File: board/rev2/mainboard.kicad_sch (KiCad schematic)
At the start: 0 parts

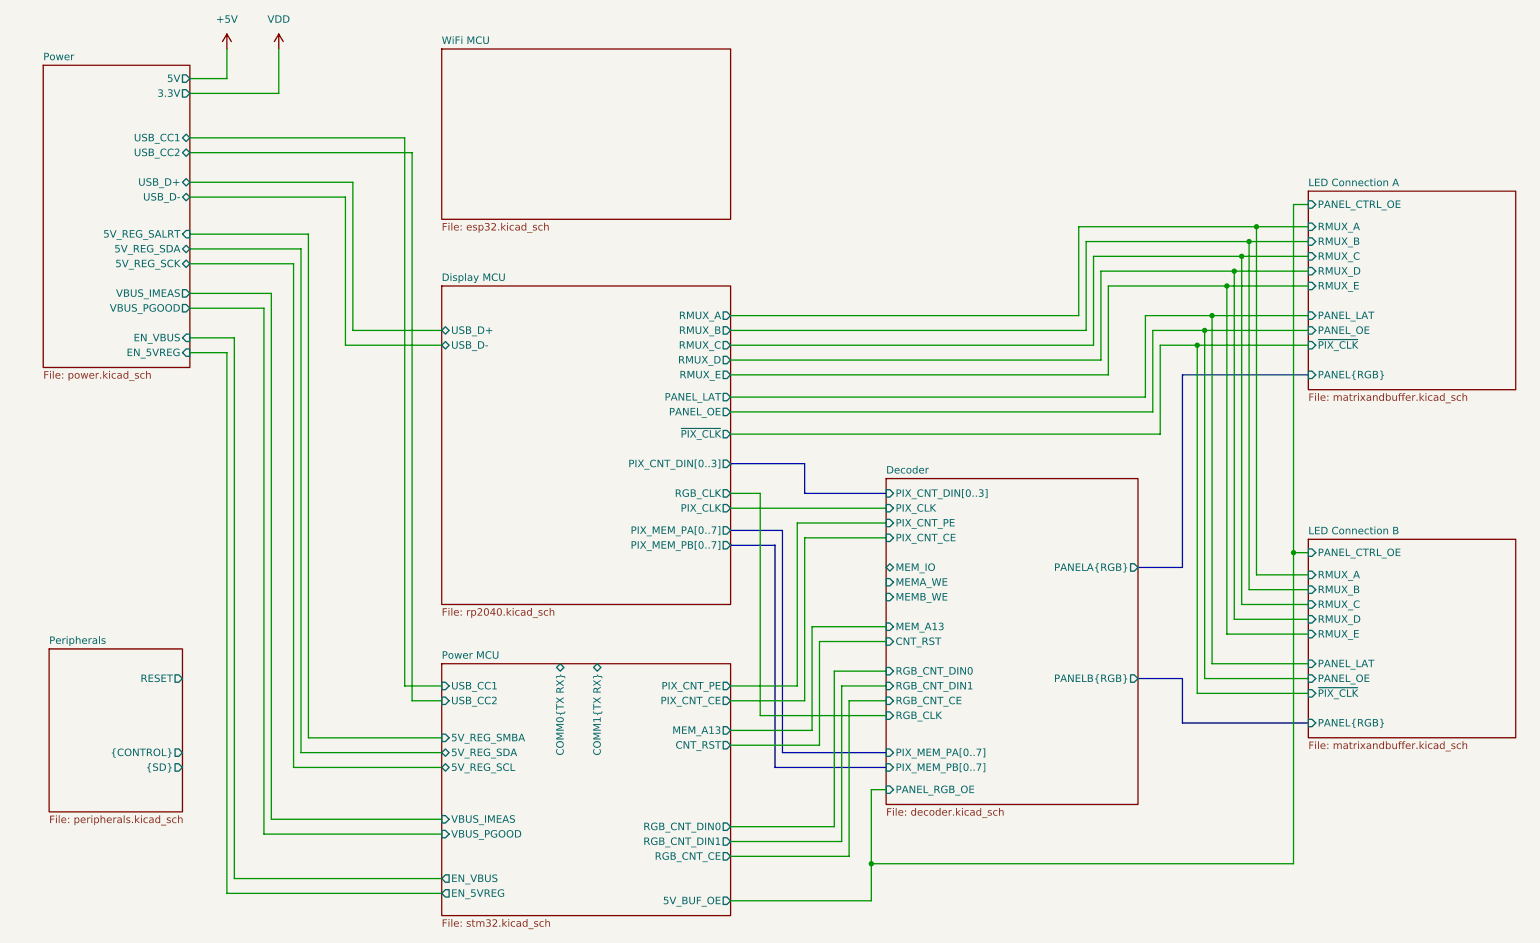
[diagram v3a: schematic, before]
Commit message: Board GPIO allocation
- and usbmux

still need to do termination on the big buses + a bunch of bypass caps
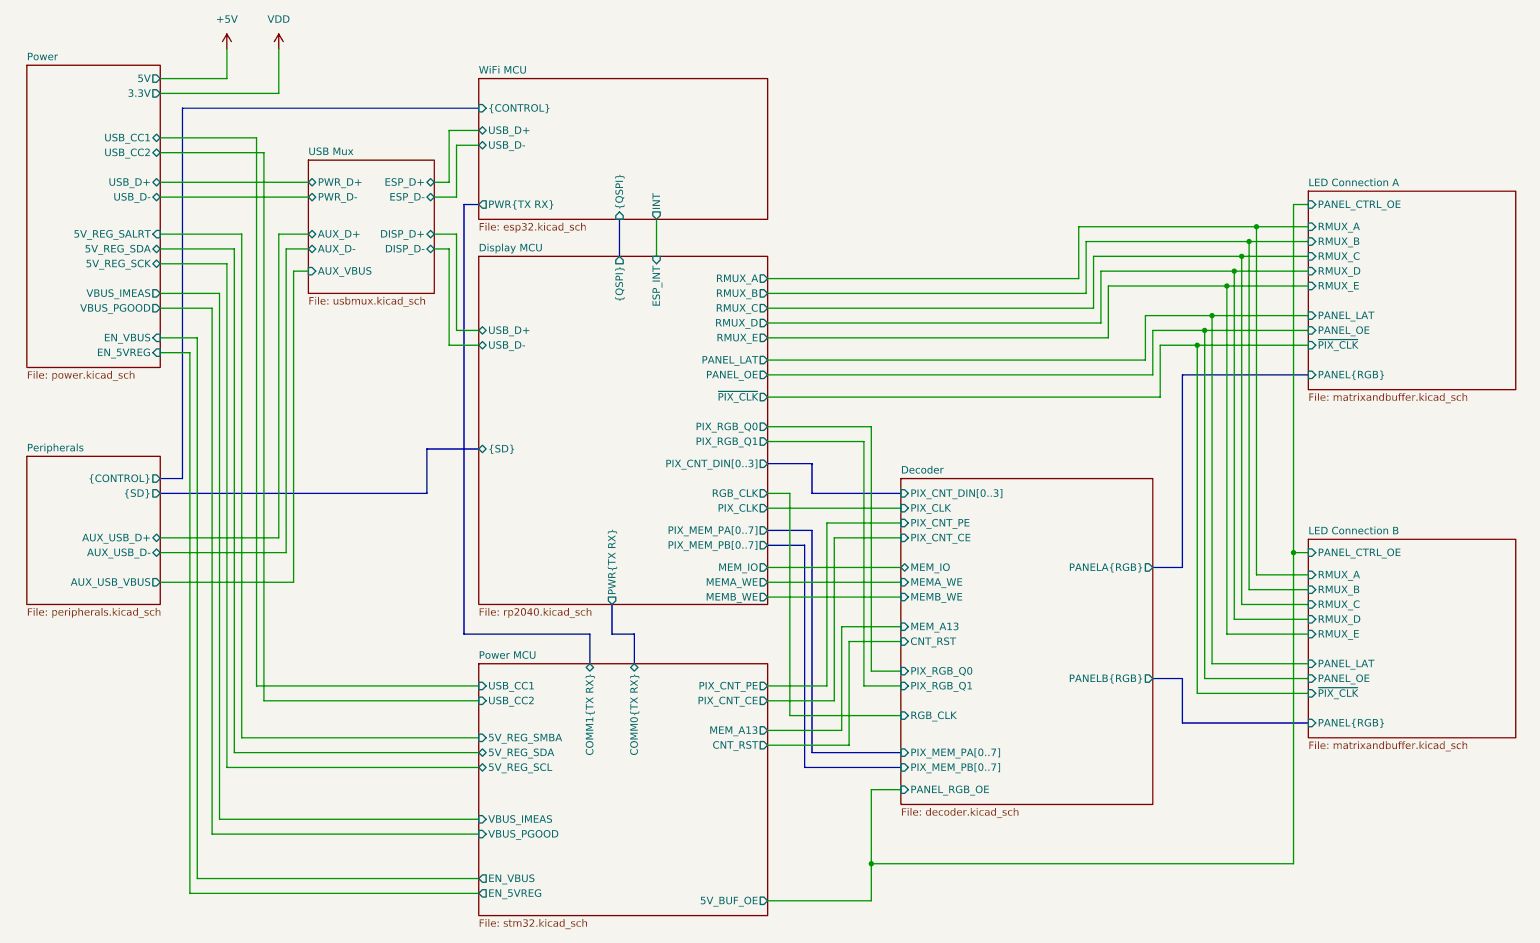
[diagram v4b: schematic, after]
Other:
- added sheet USB Mux (usbmux.kicad_sch)
- sheet Decoder ports: added PIX_RGB_Q0, PIX_RGB_Q1; removed RGB_CNT_CE, RGB_CNT_DIN0, RGB_CNT_DIN1
- sheet Display MCU ports: added ESP_INT, MEMA_WE, MEMB_WE, MEM_IO, PIX_RGB_Q0, PIX_RGB_Q1, PWR{TX RX}, {QSPI}, {SD}; removed none
- sheet Peripherals ports: added AUX_USB_D+, AUX_USB_D-, AUX_USB_VBUS; removed RESET
- sheet Power MCU ports: added none; removed RGB_CNT_CE, RGB_CNT_DIN0, RGB_CNT_DIN1
- sheet WiFi MCU ports: added INT, PWR{TX RX}, USB_D+, USB_D-, {CONTROL}, {QSPI}; removed none
- company: (none) -> MLABS
- title: (none) -> Root

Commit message: Continue board, assign caps/res, adjust for JLC availability
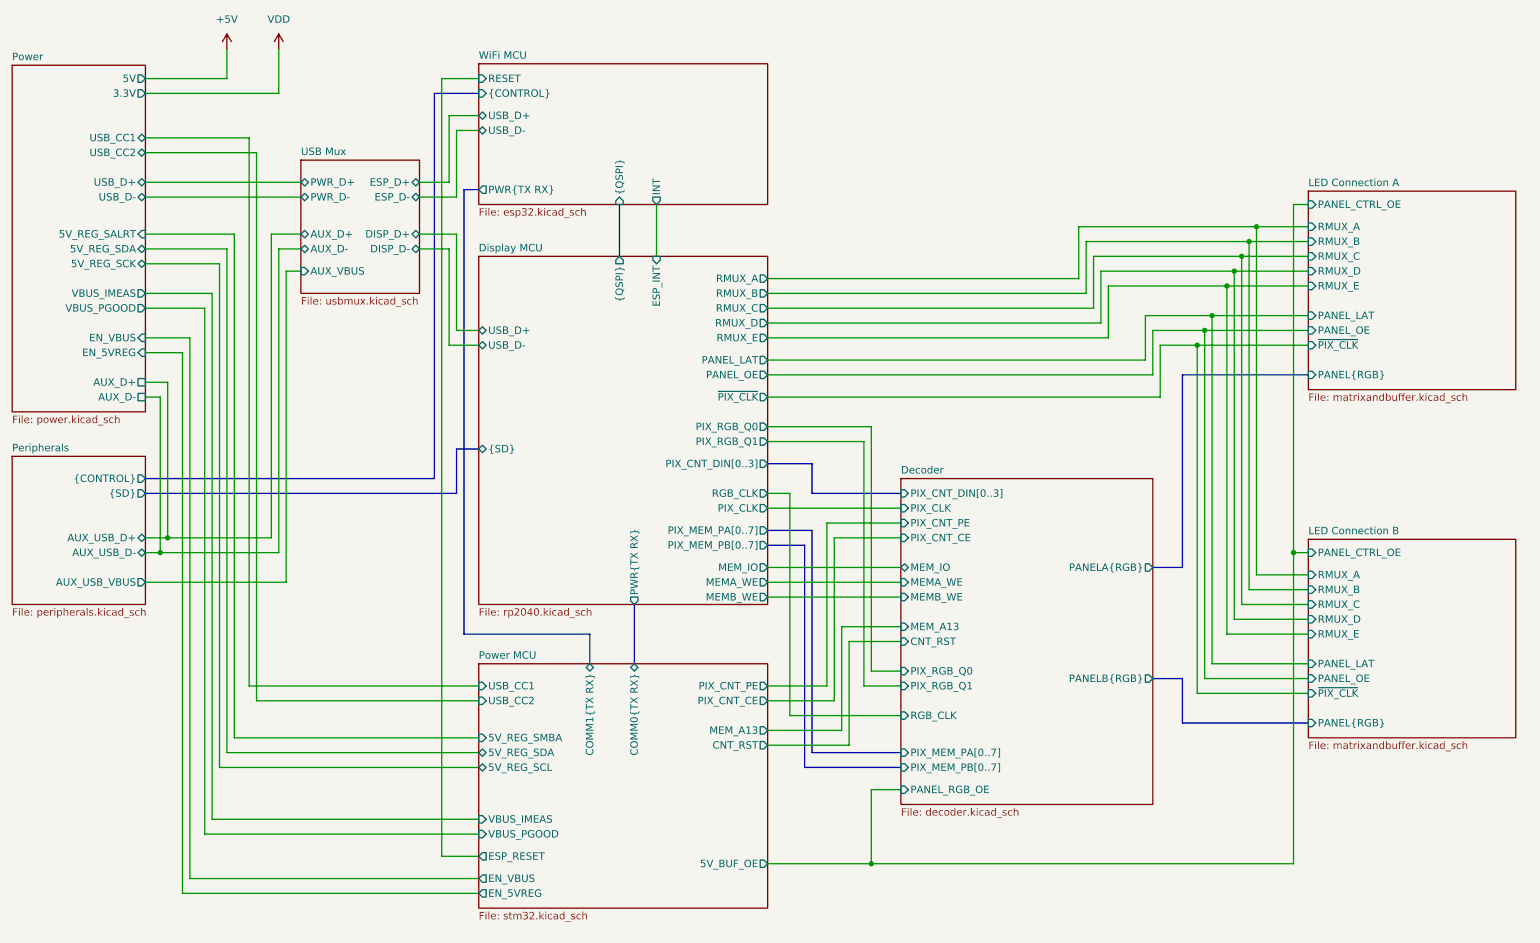
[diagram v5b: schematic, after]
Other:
- sheet Power ports: added AUX_D+, AUX_D-; removed none
- sheet Power MCU ports: added ESP_RESET; removed none
- sheet WiFi MCU ports: added RESET; removed none

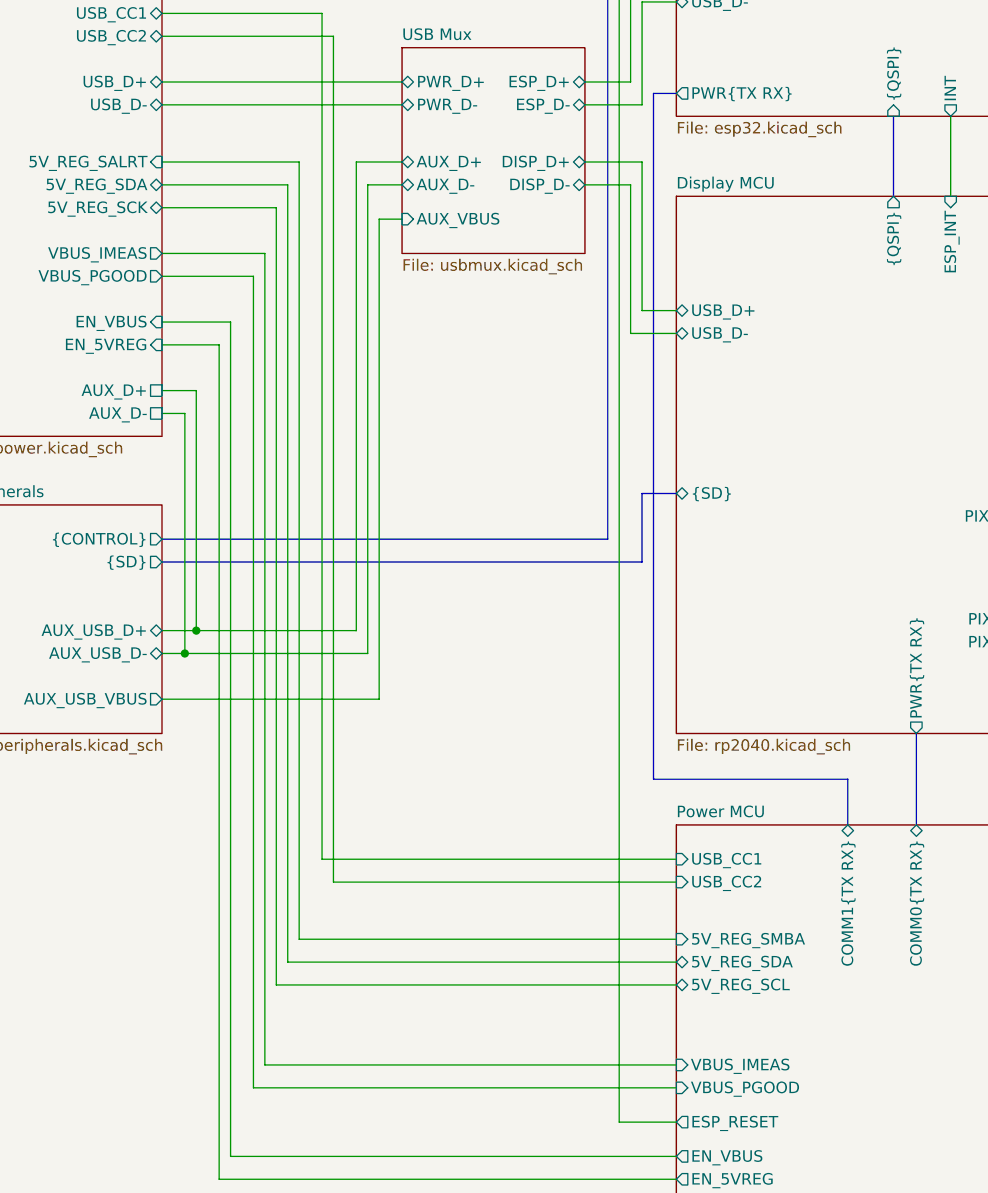
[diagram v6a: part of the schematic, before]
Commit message: Add netclasses, more footprints, fix ERC
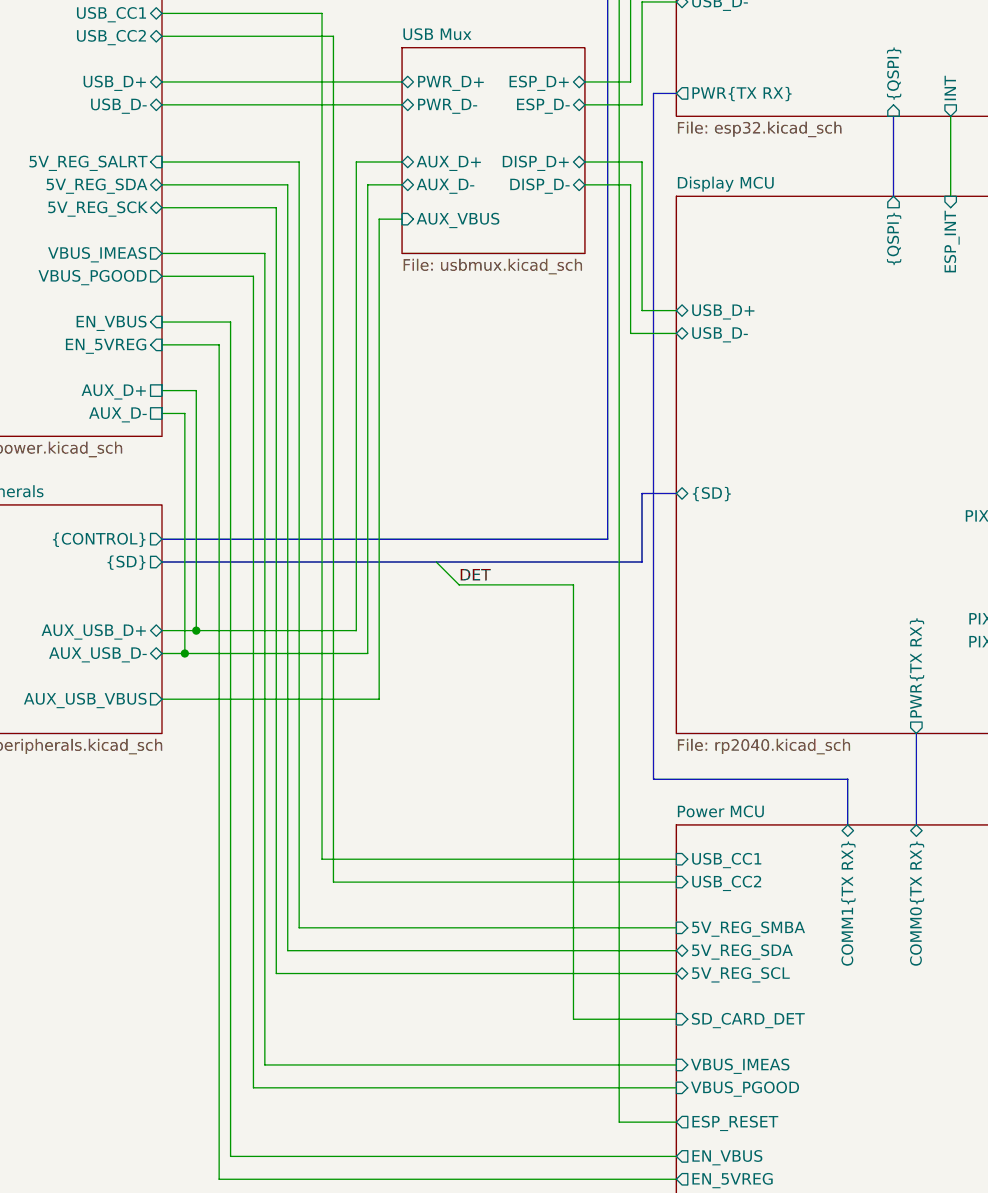
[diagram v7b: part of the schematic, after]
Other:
- sheet Power MCU ports: added SD_CARD_DET; removed none
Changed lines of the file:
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@@
 		(color 0 0 0 0)
 	)
+	(bus_entry
+		(at 68.58 97.79)
+		(size 2.54 2.54)
+		(stroke
+			(width 0)
+			(type default)
+		)
+	)
 	(wire
 		(pts
@@
 	(wire
 		(pts
-			(xy 52.07 55.88) (xy 52.07 142.24)
-		)
-		(stroke
-			(width 0)
-			(type default)
-		)
-	)
-	(wire
-		(pts
-			(xy 95.25 139.7) (xy 53.34 139.7)
+			(xy 52.07 55.88) (xy 52.07 140.97)
+		)
+		(stroke
+			(width 0)
+			(type default)
+		)
+	)
+	(wire
+		(pts
+			(xy 95.25 138.43) (xy 53.34 138.43)
 		)
 		(stroke
@@
 	(wire
 		(pts
-			(xy 52.07 142.24) (xy 95.25 142.24)
+			(xy 52.07 140.97) (xy 95.25 140.97)
 		)
 		(stroke
@@
 	(wire
 		(pts
+			(xy 83.82 148.59) (xy 95.25 148.59)
+		)
+		(stroke
+			(width 0)
+			(type default)
+		)
+	)
+	(wire
+		(pts
 			(xy 55.88 36.83) (xy 55.88 130.81)
 		)
@@
 	(wire
 		(pts
+			(xy 83.82 100.33) (xy 83.82 148.59)
+		)
+		(stroke
+			(width 0)
+			(type default)
+		)
+	)
+	(wire
+		(pts
 			(xy 162.56 128.27) (xy 162.56 86.36)
 		)
@@
 	(wire
 		(pts
-			(xy 53.34 139.7) (xy 53.34 53.34)
+			(xy 53.34 138.43) (xy 53.34 53.34)
 		)
 		(stroke
@@
 		)
 	)
+	(wire
+		(pts
+			(xy 71.12 100.33) (xy 83.82 100.33)
+		)
+		(stroke
+			(width 0)
+			(type default)
+		)
+	)
 	(bus
 		(pts
@@
 	(bus
 		(pts
+			(xy 68.58 97.79) (xy 91.44 97.79)
+		)
+		(stroke
+			(width 0)
+			(type default)
+		)
+	)
+	(bus
+		(pts
 			(xy 91.44 97.79) (xy 91.44 90.17)
 		)
@@
 	(wire
 		(pts
-			(xy 95.25 144.78) (xy 50.8 144.78)
+			(xy 95.25 143.51) (xy 50.8 143.51)
 		)
 		(stroke
@@
 	(wire
 		(pts
-			(xy 50.8 144.78) (xy 50.8 58.42)
+			(xy 50.8 143.51) (xy 50.8 58.42)
 		)
 		(stroke
@@
 	(bus
 		(pts
-			(xy 38.1 97.79) (xy 91.44 97.79)
+			(xy 38.1 97.79) (xy 68.58 97.79)
 		)
 		(stroke
@@
 			(width 0)
 			(type default)
+		)
+	)
+	(label "DET"
+		(at 71.12 100.33 0)
+		(effects
+			(font
+				(size 1.27 1.27)
+			)
+			(justify left bottom)
 		)
 	)
@@
 		)
 		(pin "5V_REG_SCL" bidirectional
-			(at 95.25 144.78 180)
+			(at 95.25 143.51 180)
 			(effects
 				(font
@@
 		)
 		(pin "5V_REG_SDA" bidirectional
-			(at 95.25 142.24 180)
+			(at 95.25 140.97 180)
 			(effects
 				(font
@@
 		)
 		(pin "5V_REG_SMBA" input
-			(at 95.25 139.7 180)
+			(at 95.25 138.43 180)
 			(effects
 				(font
@@
 			(effects
 				(font
+					(size 1.27 1.27)
+				)
+				(justify left)
+			)
+		)
+		(pin "SD_CARD_DET" input
+			(at 95.25 148.59 180)
+			(effects
+				(font
